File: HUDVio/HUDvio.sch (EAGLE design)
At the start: 61 parts, among them U1 ST_STM32F446RET7, U3 TVP5150AM1PBSR, U4 NEXPERIA_NVT2006, U5 MAXIM_MAX4389, U6 MIC_MIC5504-1.8, X1 ABRACON_ABM8-27.000MHZ, X2 ABRACON_ABM8-14.31818MHZ

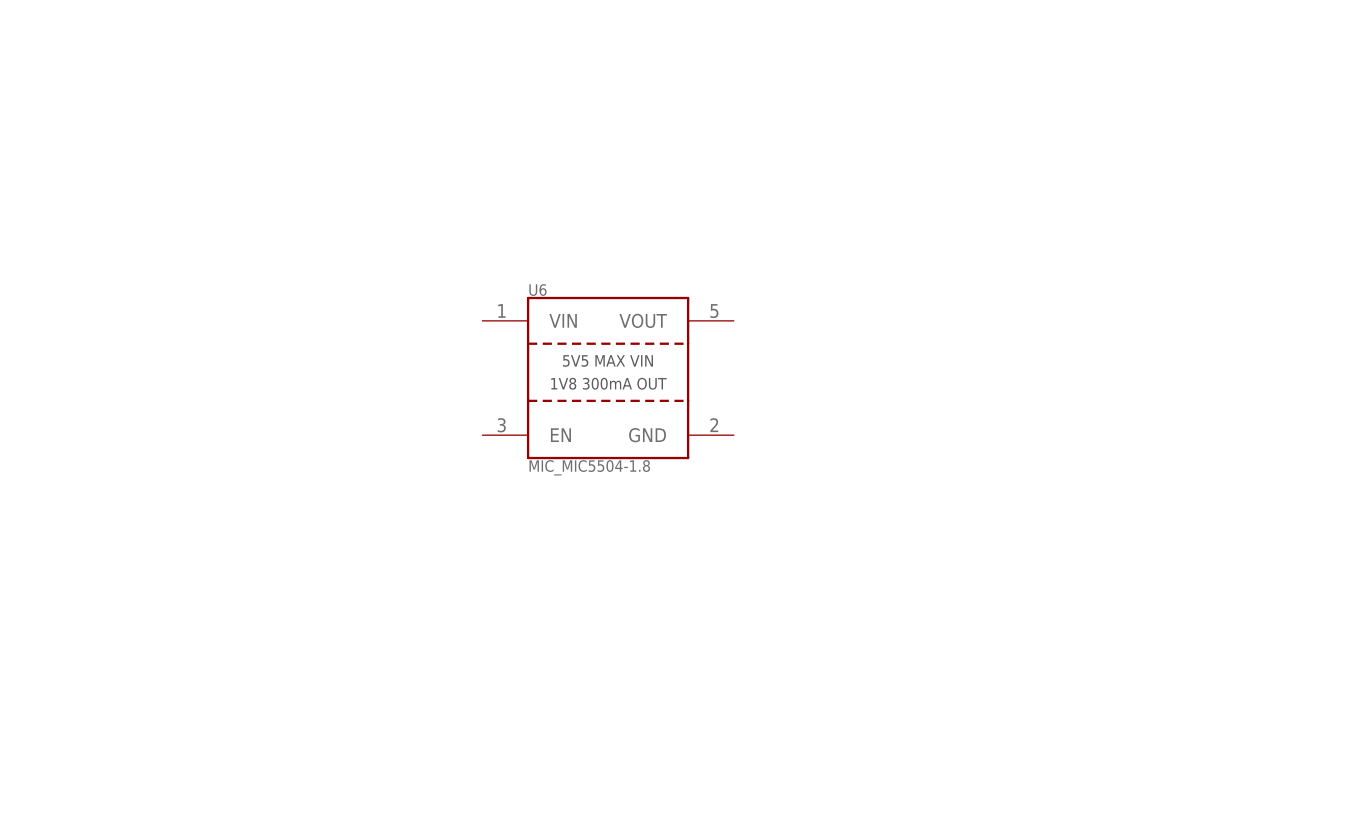
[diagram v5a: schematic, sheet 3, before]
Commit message: Schematic done, moving to Board
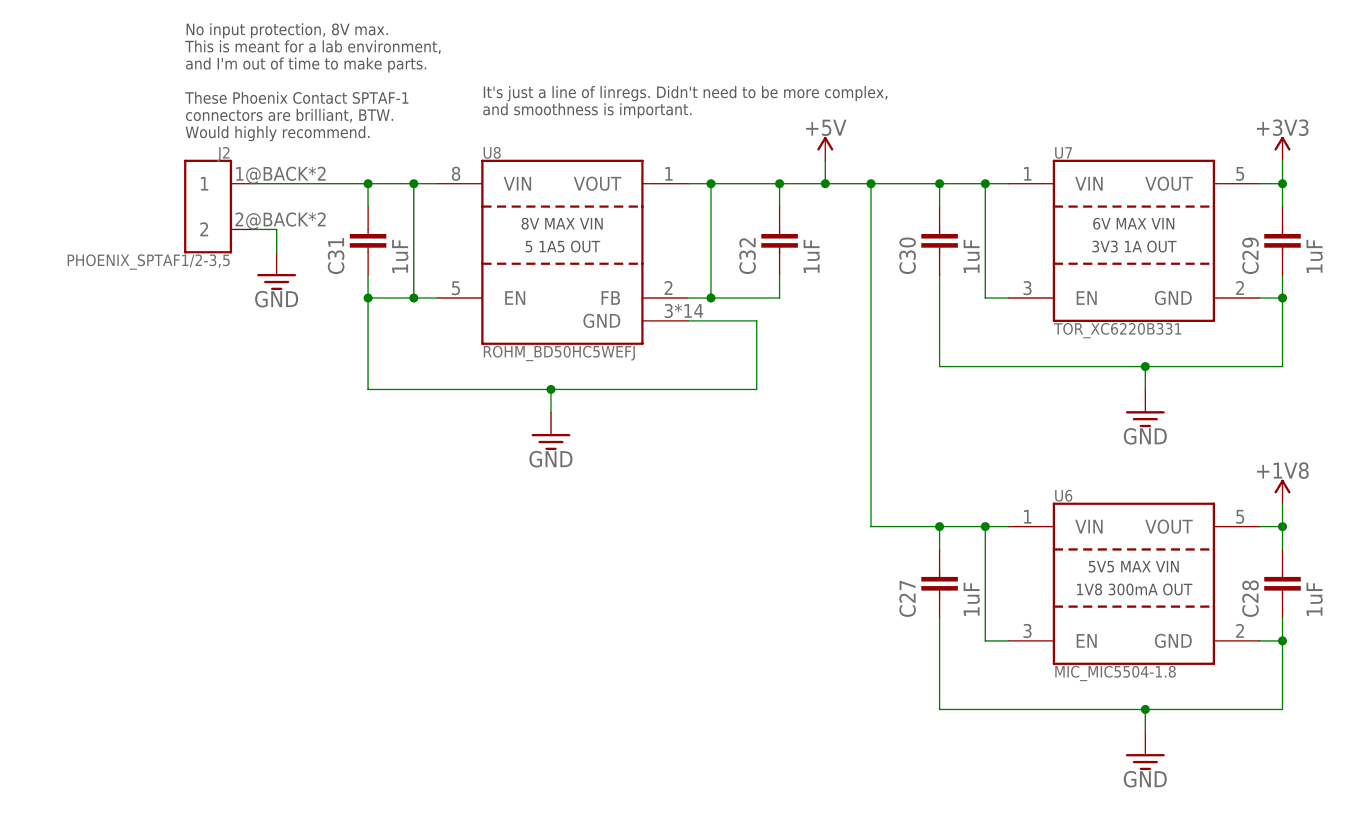
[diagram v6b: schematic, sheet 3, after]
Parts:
- added C27, C28, C29, C30, C31, C32: 1UF_0805, Skyhawkson-Capacitors:1UF_0805
- added J2: PHOENIX_SPTAF1/2-3,5, Skyhawkson-Connectors:PHOENIX_SPTAF1/2-3,5
- added U7: TOR_XC6220B331, Skyhawkson-Power:TOR_XC6220B331
- added U8: ROHM_BD50HC5WEFJ, Skyhawkson-Power:ROHM_BD50HC5WEFJ
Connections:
- new net N$19: C29.1, C30.1, U7.GND@2
- net +1V8: now also C28.2, U6.VOUT@5
- net +3V3: now also C29.2, U7.VOUT@5
- net +5V: now also C27.2, C30.2, C32.1, C32.2, U6.EN@3, U6.VIN@1, U7.EN@3, U7.VIN@1, U8.FB@2, U8.VOUT@1
- net GND: now also C27.1, C28.1, C31.1, C31.2, J2.1, J2.2, U6.GND@2, U8.EN@5, U8.GND@3,FIN, U8.VIN@8
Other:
- note added: "It's just a line of linregs. Didn't need to be more complex, and smoothness is important."
- note added: "No input protection, 8V max. This is meant for a lab environment, and I'm out of time to make parts."
- note added: "These Phoenix Contact SPTAF-1 connectors are brilliant, BTW. Would highly recommend."
- moved on the sheet: R11, U6

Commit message: Schematic Complete
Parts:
- added U$30: SWD_HEADER, Skyhawkson-Connectors:SWD_HEADER
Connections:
- removed net N$16: S1.2, U1.!RST!@7
- new net !RST: S1.2, U$30.!RST!@10, U1.!RST!@7
- new net SWCLK: U$30.SWCLK@4, U1.PA14@49
- new net SWDIO: U$30.SWDIO@2, U1.PA13@46
- net +3V3: now also U$30.VCC@1
- net GND: now also U$30.GND@3, U$30.GND@5, U$30.GNDDT@9
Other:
- note added: "SWD Header"
- moved on the sheet: C22, C23, C24, C25, C26, R20, R21, R22, S1, U1
